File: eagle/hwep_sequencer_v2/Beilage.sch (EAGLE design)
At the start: 175 parts, among them X1 ESP32-AZDEL

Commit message: Board: Bedruck Formatiert
Board Optimiert und Layer:
Names
Values
Formatiert
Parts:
- C1: CATEGORY (none) -> 2
- D1, D14, D16, D4: CATEGORY (none) -> 13
- X1: CATEGORY (none) -> 18
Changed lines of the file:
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@@
 <part name="GND78" library="supply_GruS" library_urn="urn:adsk.eagle:library:13579815" deviceset="GND" device=""/>
 <part name="+3V55" library="supply_GruS" library_urn="urn:adsk.eagle:library:13579815" deviceset="+3V3" device=""/>
-<part name="D1" library="74xx_GruS" library_urn="urn:adsk.eagle:library:13569359" deviceset="74*138" device="N" package3d_urn="urn:adsk.eagle:package:33482861/2" technology="AHC"/>
-<part name="X1" library="modul_GruS" library_urn="urn:adsk.eagle:library:13580331" deviceset="ESP32" device="-AZDEL" package3d_urn="urn:adsk.eagle:package:33485844/4"/>
+<part name="D1" library="74xx_GruS" library_urn="urn:adsk.eagle:library:13569359" deviceset="74*138" device="N" package3d_urn="urn:adsk.eagle:package:33482861/2" technology="AHC">
+<attribute name="CATEGORY" value="13"/>
+</part>
+<part name="X1" library="modul_GruS" library_urn="urn:adsk.eagle:library:13580331" deviceset="ESP32" device="-AZDEL" package3d_urn="urn:adsk.eagle:package:33485844/5">
+<attribute name="CATEGORY" value="18"/>
+</part>
 <part name="+3V10" library="supply_GruS" library_urn="urn:adsk.eagle:library:13579815" deviceset="+3V3" device=""/>
 <part name="GND25" library="supply_GruS" library_urn="urn:adsk.eagle:library:13579815" deviceset="GND" device=""/>
-<part name="C1" library="rcl_GruS" library_urn="urn:adsk.eagle:library:13572313" deviceset="C-EU" device="C0805" package3d_urn="urn:adsk.eagle:package:23617/2" value="1u"/>
-<part name="D4" library="74xx_GruS" library_urn="urn:adsk.eagle:library:13569359" deviceset="74*1G125" device="DBV" package3d_urn="urn:adsk.eagle:package:33442082/1" technology="AHC"/>
+<part name="C1" library="rcl_GruS" library_urn="urn:adsk.eagle:library:13572313" deviceset="C-EU" device="C0805" package3d_urn="urn:adsk.eagle:package:23617/2" value="1u">
+<attribute name="CATEGORY" value="2"/>
+</part>
+<part name="D4" library="74xx_GruS" library_urn="urn:adsk.eagle:library:13569359" deviceset="74*1G125" device="DBV" package3d_urn="urn:adsk.eagle:package:33442082/1" technology="AHC">
+<attribute name="CATEGORY" value="13"/>
+</part>
 <part name="+3V17" library="supply_GruS" library_urn="urn:adsk.eagle:library:13579815" deviceset="+3V3" device=""/>
 <part name="GND26" library="supply_GruS" library_urn="urn:adsk.eagle:library:13579815" deviceset="GND" device=""/>
@@
 <part name="R46" library="rcl_GruS" library_urn="urn:adsk.eagle:library:13572313" deviceset="R-EUS" device="R0805" package3d_urn="urn:adsk.eagle:package:18365371/1" value="10k"/>
 <part name="+3V57" library="supply_GruS" library_urn="urn:adsk.eagle:library:13579815" deviceset="+3V3" device=""/>
-<part name="D16" library="74xx_GruS" library_urn="urn:adsk.eagle:library:13569359" deviceset="74*1G04" device="DBV" package3d_urn="urn:adsk.eagle:package:33442082/1" technology="AHC"/>
-<part name="D14" library="74xx_GruS" library_urn="urn:adsk.eagle:library:13569359" deviceset="74*1G04" device="DBV" package3d_urn="urn:adsk.eagle:package:33442082/1" technology="AHC"/>
+<part name="D16" library="74xx_GruS" library_urn="urn:adsk.eagle:library:13569359" deviceset="74*1G04" device="DBV" package3d_urn="urn:adsk.eagle:package:33442082/1" technology="AHC">
+<attribute name="CATEGORY" value="13"/>
+</part>
+<part name="D14" library="74xx_GruS" library_urn="urn:adsk.eagle:library:13569359" deviceset="74*1G04" device="DBV" package3d_urn="urn:adsk.eagle:package:33442082/1" technology="AHC">
+<attribute name="CATEGORY" value="13"/>
+</part>
 <part name="C16" library="rcl_GruS" library_urn="urn:adsk.eagle:library:13572313" deviceset="C-EU" device="C0805" package3d_urn="urn:adsk.eagle:package:23617/2" value="100n">
 <attribute name="CATEGORY" value="2"/>
@@
 <attribute name="NAME" x="59.69" y="238.76" size="1.6764" layer="95" font="vector" align="bottom-center"/>
 <attribute name="VALUE" x="59.69" y="236.982" size="1.27" layer="96" font="vector" align="bottom-center"/>
+<attribute name="CATEGORY" x="45.72" y="233.68" size="1.778" layer="96" display="off"/>
 </instance>
 <instance part="X1" gate="G$1" x="91.44" y="187.96" smashed="yes">
 <attribute name="NAME" x="119.38" y="193.04" size="1.6764" layer="95" font="vector" align="bottom-center"/>
 <attribute name="VALUE" x="119.38" y="191.262" size="1.27" layer="96" font="vector" align="bottom-center"/>
+<attribute name="CATEGORY" x="91.44" y="187.96" size="1.778" layer="96" display="off"/>
 </instance>
 <instance part="+3V10" gate="G$1" x="40.64" y="238.76" smashed="yes">
@@
 <attribute name="NAME" x="77.724" y="217.9066" size="1.6764" layer="95" font="vector" align="bottom-right"/>
 <attribute name="VALUE" x="77.724" y="215.1126" size="1.27" layer="96" font="vector" align="bottom-right"/>
+<attribute name="CATEGORY" x="78.74" y="218.44" size="1.778" layer="96" display="off"/>
 </instance>
 <instance part="D4" gate="G$1" x="35.56" y="101.6" smashed="yes" rot="R180">
 <attribute name="NAME" x="35.56" y="109.22" size="1.6764" layer="95" font="vector" align="bottom-center"/>
 <attribute name="VALUE" x="35.56" y="107.442" size="1.27" layer="96" font="vector" align="bottom-center"/>
+<attribute name="CATEGORY" x="35.56" y="101.6" size="1.778" layer="96" display="off"/>
 </instance>
 <instance part="D4" gate="P" x="121.92" y="243.84" smashed="yes">
@@
 <attribute name="NAME" x="48.26" y="76.835" size="1.6764" layer="95" font="vector" align="bottom-center"/>
 <attribute name="VALUE" x="48.26" y="74.422" size="1.27" layer="96" font="vector" align="bottom-center"/>
+<attribute name="CATEGORY" x="48.26" y="68.58" size="1.778" layer="96" display="off"/>
 </instance>
 <instance part="D16" gate="G$2" x="165.1" y="71.12" smashed="yes">
@@
 <attribute name="NAME" x="48.26" y="191.135" size="1.6764" layer="95" font="vector" align="bottom-center"/>
 <attribute name="VALUE" x="48.26" y="188.722" size="1.27" layer="96" font="vector" align="bottom-center"/>
+<attribute name="CATEGORY" x="48.26" y="182.88" size="1.778" layer="96" display="off"/>
 </instance>
 <instance part="D14" gate="G$2" x="149.86" y="187.96" smashed="yes">

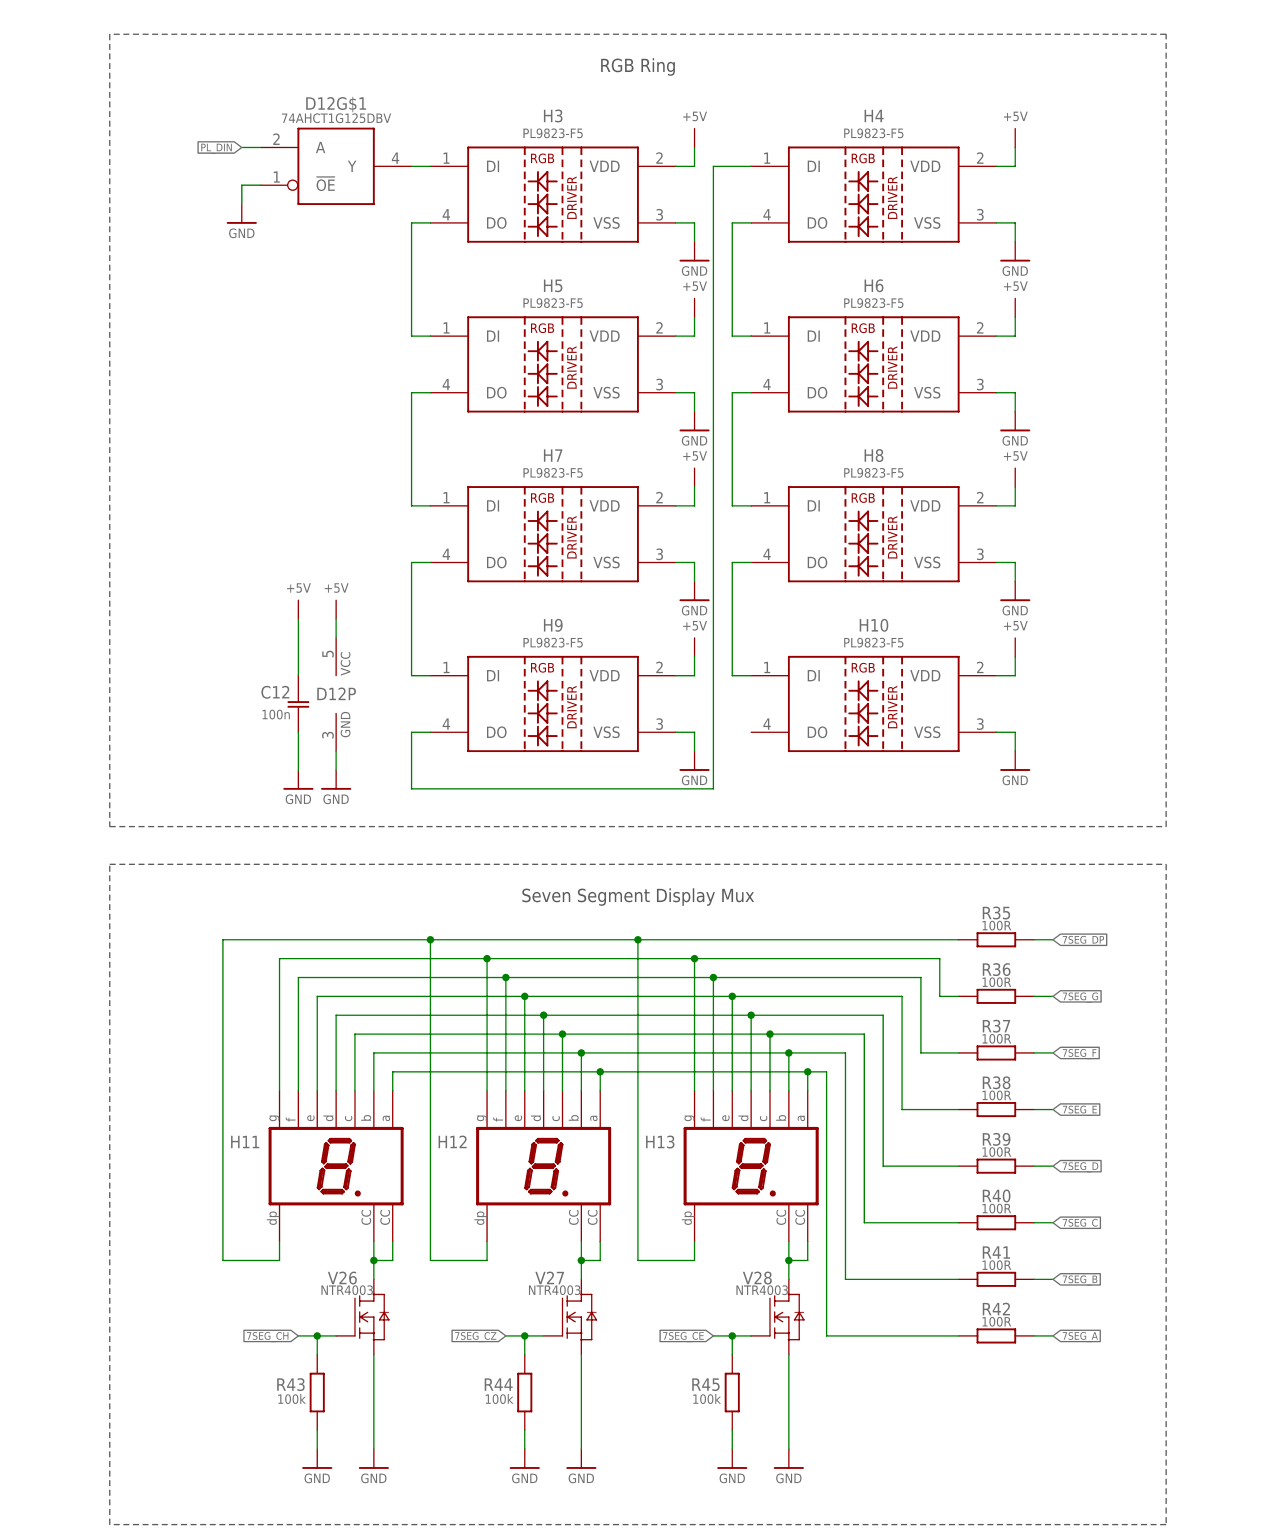
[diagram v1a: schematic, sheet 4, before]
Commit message: Board Prototyp Fertiggestellt
Fehlende Entkoppel-Kondensatoren eingefügt
Bestückungsdruck überarbeitet und Formatiert
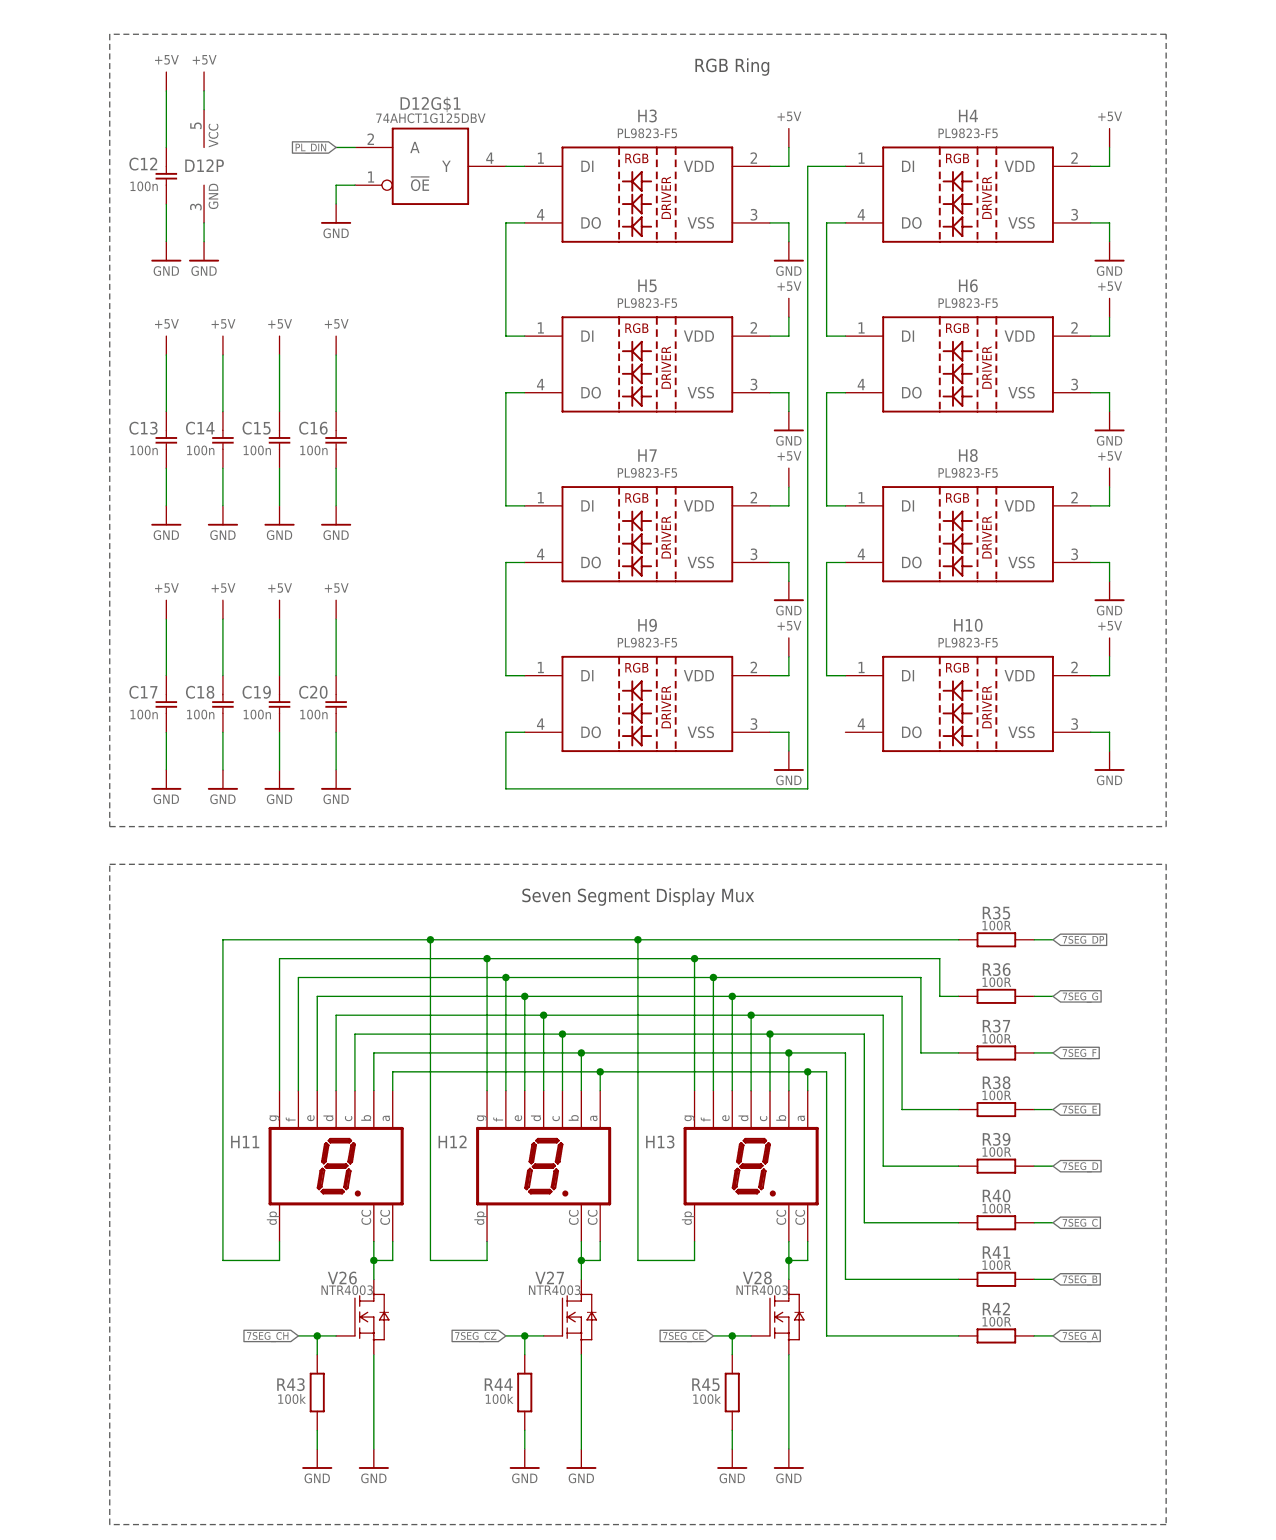
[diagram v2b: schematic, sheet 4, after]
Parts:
- added C21, C22, C25, C26: 1u, rcl_GruS:C-EUC0805
- added C23, C24, C27, C28: 100n, rcl_GruS:C-EUC0805
- C13, C14, C17, C18: value 1u -> 100n
- R13: value 10k -> 56k; device rcl_GruS:P160L -> rcl_GruS:R-EUSR0805
- R2: device rcl_GruS:R-EUSR0805 -> rcl_GruS:P160L
- R20: value 56k -> 10k
- R6: value 10k -> 330R; device rcl_GruS:P160L -> rcl_GruS:R-EUSR0805
- R8: value 330R -> 1M
- R9: value 1M -> 10k; device rcl_GruS:R-EUSR0805 -> rcl_GruS:P160L
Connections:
- net +3V3: now also C21.1, C22.1, C23.1, C24.1, C25.1, C26.1, C27.1, C28.1, R17.2, R9.2; no longer C13.1, C14.1, C15.1, C16.1, C17.1, C18.1, C19.1, C20.1, R13.2, R6.2
- net +5V: now also C13.1, C14.1, C15.1, C16.1, C17.1, C18.1, C19.1, C20.1
- net 088S052_!CS!: now also R20.1; no longer R1.1
- net 23S08_!CS: now also R1.1; no longer R2.1
- net ADC0: now also R2.3; no longer R3.3
- net ADC1: now also R3.3; no longer R4.3
- net ADC2: now also R4.3; no longer R5.3
- net ADC3: now also R5.3; no longer R6.3
- net ADC4: now also R9.3; no longer R10.3
- net ADC5: now also R10.3; no longer R11.3
- net ADC6: now also R11.3; no longer R12.3
- net ADC7: now also R12.3; no longer R13.3
- net CLRR: now also R16.2; no longer R17.2
- net EC11_A: now also R17.1; no longer R18.1
- net EC11_B: now also R18.1; no longer R19.1
- net EC11_SW: now also R19.1; no longer R20.1
- net EVENT: now also R15.2, R8.2; no longer R16.2, R9.2
- net GND: now also C21.2, C22.2, C23.2, C24.2, C25.2, C26.2, C27.2, C28.2, R2.1, R7.1; no longer R17.1, R6.1
- net N$58: now also R6.2; no longer R7.2
- net N$60: now also R6.1; no longer R7.1
- net N$9: now also R7.2; no longer R8.2
- net PAUSE_CNT: now also R13.2; no longer R14.2
- net RESET_CNT: now also R14.2; no longer R15.2
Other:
- moved on the sheet: C1, C12, C2, C3, D1, D12G$1, D12P, D2, D3, D4G$1, H10, H3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
